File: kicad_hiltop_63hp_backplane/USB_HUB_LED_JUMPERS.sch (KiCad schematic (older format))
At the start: 81 parts, among them J12 4POS_JUMPER, J13 4POS_JUMPER, J14 4POS_JUMPER, J15 4POS_JUMPER, J16 4POS_JUMPER, U5 USB2517, Y2 24Mhz Xtal

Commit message: Rev A
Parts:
- C38, C39, C40, C41, C42, C43, C44, C45, C46, C47, C48, C50, C51, C52, C53: symbol device:C -> hiltop_backplane_brd-rescue:C-device; Devtank (none) -> 105-002
- C49, C54: symbol device:C -> hiltop_backplane_brd-rescue:C-device; Devtank (none) -> 105-014
- D10, D11, D12, D13, D6, D7, D8, D9: value LED -> LED RED; symbol device:LED -> hiltop_backplane_brd-rescue:LED-device; Devtank (none) -> 110-004
- D14, D16, D18, D20, D22, D24, D26: value GRN -> LED GRN; symbol device:LED -> hiltop_backplane_brd-rescue:LED-device; Devtank (none) -> 110-005
- D15, D17, D19, D21, D23, D25, D27: value YEL -> LED YEL; symbol device:LED -> hiltop_backplane_brd-rescue:LED-device; Devtank (none) -> 110-007
- D5: symbol ESD_Protection:NUP2105L -> hiltop_backplane_brd-rescue:NUP2105L-ESD_Protection; Devtank (none) -> 136-002
- J12, J13, J14, J15, J16: symbol gti_Lattice:4POS_JUMPER -> hiltop_backplane_brd-rescue:4POS_JUMPER-gti_Lattice; Devtank (none) -> 711-003
- R48, R49: symbol device:R -> hiltop_backplane_brd-rescue:R-device; Devtank (none) -> 101-015
- R50, R51, R53, R54, R57, R58: symbol device:R -> hiltop_backplane_brd-rescue:R-device; Devtank (none) -> 101-010
- R52: symbol device:R -> hiltop_backplane_brd-rescue:R-device; Devtank (none) -> 101-050
- R55, R56, R59: symbol device:R -> hiltop_backplane_brd-rescue:R-device
- R60, R61, R62, R63, R64, R65, R66, R67, R68, R69, R70, R71, R72, R73, R74, R75, R76, R77, R78, R79, R80, R81: symbol device:R -> hiltop_backplane_brd-rescue:R-device; Devtank (none) -> 101-509
- U5: symbol Devtank:USB2517 -> hiltop_backplane_brd-rescue:USB2517-Devtank; Devtank (none) -> 118-004
- Y2: symbol device:Crystal -> hiltop_backplane_brd-rescue:Crystal-device; Devtank (none) -> 181-003

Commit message: add latest changes
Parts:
- removed D5: NUP2105L, Package_TO_SOT_SMD:SOT-23, symbol hiltop_backplane_brd-rescue:NUP2105L-ESD_Protection
- C38, C43, C44, C45, C46, C47, C48, C49, C50, C51, C52, C53, C54: symbol hiltop_backplane_brd-rescue:C-device -> hiltop_backplane_brd-rescue:C-device-hiltop_backplane_brd-rescue
- C39: value 100nF -> 18pF; symbol hiltop_backplane_brd-rescue:C-device -> hiltop_backplane_brd-rescue:C-device-hiltop_backplane_brd-rescue; Devtank 105-002 -> (none)
- C40, C41: value 100nF -> 1uF; symbol hiltop_backplane_brd-rescue:C-device -> hiltop_backplane_brd-rescue:C-device-hiltop_backplane_brd-rescue; Devtank 105-002 -> (none)
- C42: value 100nF -> 18pF; symbol hiltop_backplane_brd-rescue:C-device -> hiltop_backplane_brd-rescue:C-device-hiltop_backplane_brd-rescue
- D10, D11, D12, D13, D14, D15, D16, D17, D18, D19, D20, D21, D22, D23, D24, D25, D26, D27, D6, D7, D8, D9: symbol hiltop_backplane_brd-rescue:LED-device -> hiltop_backplane_brd-rescue:LED-device-hiltop_backplane_brd-rescue
- J12, J13, J14, J15, J16: symbol hiltop_backplane_brd-rescue:4POS_JUMPER-gti_Lattice -> hiltop_backplane_brd-rescue:4POS_JUMPER-gti_Lattice-hiltop_backplane_brd-rescue
- R48: value 100K -> 0R; symbol hiltop_backplane_brd-rescue:R-device -> hiltop_backplane_brd-rescue:R-device-hiltop_backplane_brd-rescue
- R49, R50, R52, R53, R54, R55, R56, R57, R58, R59, R60, R61, R62, R63, R64, R65, R66, R67, R68, R69, R70, R71, R72, R73, R74, R75, R76, R77, R78, R79, R80, R81: symbol hiltop_backplane_brd-rescue:R-device -> hiltop_backplane_brd-rescue:R-device-hiltop_backplane_brd-rescue
- R51: value 10K -> 1M; symbol hiltop_backplane_brd-rescue:R-device -> hiltop_backplane_brd-rescue:R-device-hiltop_backplane_brd-rescue; Devtank 101-010 -> (none)
- U5: symbol hiltop_backplane_brd-rescue:USB2517-Devtank -> hiltop_backplane_brd-rescue:USB2517-Devtank-hiltop_backplane_brd-rescue
- Y2: symbol hiltop_backplane_brd-rescue:Crystal-device -> hiltop_backplane_brd-rescue:Crystal-device-hiltop_backplane_brd-rescue
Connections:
- wire segments 290 -> 285

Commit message: started simplifications to design
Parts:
- removed J12, J13, J14, J15, J16: 4POS_JUMPER, Connector_PinHeader_2.00mm:PinHeader_2x02_P2.00mm_Vertical, symbol hiltop_backplane_brd-rescue:4POS_JUMPER-gti_Lattice-hiltop_backplane_brd-rescue
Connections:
- net labels removed: EXT_SPI_MISO, EXT_SPI_MOSI, EXT_SPI_SCK, EXT_SPI_SS, FPGA_SPI_DATA1, FPGA_SPI_DATA2, FPGA_SPI_SCK, FPGA_SPI_SDI, FPGA_SPI_SDO, FPGA_SPI_SS, FTDI_AD0_SCK, FTDI_AD1_MOSI, FTDI_AD2_MISO, FTDI_AD3_SS, s_FLASH_MISO, s_FLASH_MOSI, s_FLASH_SCK, s_FLASH_SS
- wire segments 285 -> 265
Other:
- note removed: "Config 1 "="\nFTDI SPI --->FLASH SPI\nEXT SPI ---> FPGA SPI\n\nConfig 2 "||"\nFTDI SPI ---> EXT SPI\nFLASH SPI ---> FPGA SPI"
- note removed: "Switch (FPGA) Master to Slave (M/M)\n"
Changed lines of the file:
@@
 EESchema Schematic File Version 4
-LIBS:hiltop_backplane_brd-cache
-EELAYER 29 0
+EELAYER 30 0
 EELAYER END
 $Descr A4 11693 8268
@@
 Wire Wire Line
 	5625 7250 5425 7250
-$Comp
-L hiltop_backplane_brd-rescue:4POS_JUMPER-gti_Lattice-hiltop_backplane_brd-rescue J12
-U 1 1 5A304A10
-P 3100 5800
-F 0 "J12" H 3100 5800 39  0000 C CNN
-F 1 "4POS_JUMPER" H 3100 5750 39  0000 C CNN
-F 2 "Connector_PinHeader_2.00mm:PinHeader_2x02_P2.00mm_Vertical" H 3100 5800 39  0001 C CNN
-F 3 "" H 3100 5800 39  0001 C CNN
-F 4 "711-003" H 0   0   50  0001 C CNN "Devtank"
-	1    3100 5800
-	1    0    0    -1
-$EndComp
-$Comp
-L hiltop_backplane_brd-rescue:4POS_JUMPER-gti_Lattice-hiltop_backplane_brd-rescue J13
-U 1 1 5A304A17
-P 3100 6150
-F 0 "J13" H 3100 6150 39  0000 C CNN
-F 1 "4POS_JUMPER" H 3100 6100 39  0000 C CNN
-F 2 "Connector_PinHeader_2.00mm:PinHeader_2x02_P2.00mm_Vertical" H 3100 6150 39  0001 C CNN
-F 3 "" H 3100 6150 39  0001 C CNN
-F 4 "711-003" H 0   0   50  0001 C CNN "Devtank"
-	1    3100 6150
-	1    0    0    -1
-$EndComp
-$Comp
-L hiltop_backplane_brd-rescue:4POS_JUMPER-gti_Lattice-hiltop_backplane_brd-rescue J14
-U 1 1 5A304A1E
-P 3100 6550
-F 0 "J14" H 3100 6550 39  0000 C CNN
-F 1 "4POS_JUMPER" H 3100 6500 39  0000 C CNN
-F 2 "Connector_PinHeader_2.00mm:PinHeader_2x02_P2.00mm_Vertical" H 3100 6550 39  0001 C CNN
-F 3 "" H 3100 6550 39  0001 C CNN
-F 4 "711-003" H 0   0   50  0001 C CNN "Devtank"
-	1    3100 6550
-	1    0    0    -1
-$EndComp
-$Comp
-L hiltop_backplane_brd-rescue:4POS_JUMPER-gti_Lattice-hiltop_backplane_brd-rescue J15
-U 1 1 5A304A25
-P 3100 6950
-F 0 "J15" H 3100 6950 39  0000 C CNN
-F 1 "4POS_JUMPER" H 3100 6900 39  0000 C CNN
-F 2 "Connector_PinHeader_2.00mm:PinHeader_2x02_P2.00mm_Vertical" H 3100 6950 39  0001 C CNN
-F 3 "" H 3100 6950 39  0001 C CNN
-F 4 "711-003" H 0   0   50  0001 C CNN "Devtank"
-	1    3100 6950
-	1    0    0    -1
-$EndComp
-Wire Wire Line
-	2700 7100 2850 7100
-Wire Wire Line
-	2700 6700 2850 6700
-Wire Wire Line
-	2700 5950 2850 5950
-Wire Wire Line
-	2700 6300 2850 6300
-Wire Wire Line
-	3350 5950 3500 5950
-Wire Wire Line
-	3350 6300 3500 6300
-Wire Wire Line
-	3350 6700 3500 6700
-Wire Wire Line
-	3350 7100 3500 7100
-Wire Wire Line
-	2700 6050 2850 6050
-Wire Wire Line
-	3350 6050 3950 6050
-Wire Wire Line
-	2700 6400 2850 6400
-Wire Wire Line
-	3350 6400 3950 6400
-Wire Wire Line
-	2700 6800 2850 6800
-Wire Wire Line
-	3350 6800 3500 6800
-Wire Wire Line
-	2700 7200 2850 7200
-Wire Wire Line
-	3350 7200 3500 7200
-$Comp
-L hiltop_backplane_brd-rescue:4POS_JUMPER-gti_Lattice-hiltop_backplane_brd-rescue J16
-U 1 1 5A304A44
-P 3100 7450
-F 0 "J16" H 3100 7450 39  0000 C CNN
-F 1 "4POS_JUMPER" H 3100 7400 39  0000 C CNN
-F 2 "Connector_PinHeader_2.00mm:PinHeader_2x02_P2.00mm_Vertical" H 3100 7450 39  0001 C CNN
-F 3 "" H 3100 7450 39  0001 C CNN
-F 4 "711-003" H 0   0   50  0001 C CNN "Devtank"
-	1    3100 7450
-	1    0    0    -1
-$EndComp
-Wire Wire Line
-	2850 7600 2700 7600
-Wire Wire Line
-	3350 7600 3950 7600
-Wire Wire Line
-	3350 7700 3500 7700
-Wire Wire Line
-	2850 7700 2225 7700
-Text Notes 3750 7400 2    39   ~ 0
-Switch (FPGA) Master to Slave (M/M)\n
-Text Notes 875  7000 0    60   ~ 0
-Config 1 "="\nFTDI SPI --->FLASH SPI\nEXT SPI ---> FPGA SPI\n\nConfig 2 "||"\nFTDI SPI ---> EXT SPI\nFLASH SPI ---> FPGA SPI
 Text HLabel 5425 6050 0    39   Input Italic 8
 LED1
@@
 Text HLabel 5425 7250 0    39   Input Italic 8
 LED7
-Text HLabel 2700 5950 0    39   Input ~ 0
-FTDI_AD2_MISO
-Text HLabel 2700 6050 0    39   Input ~ 0
-EXT_SPI_MISO
-Text HLabel 2700 6300 0    39   Input ~ 0
-FTDI_AD1_MOSI
-Text HLabel 2700 6400 0    39   Input ~ 0
-EXT_SPI_MOSI
-Text HLabel 2700 6700 0    39   Input ~ 0
-FTDI_AD0_SCK
-Text HLabel 2700 6800 0    39   Input ~ 0
-EXT_SPI_SCK
-Text HLabel 2700 7100 0    39   Input ~ 0
-FTDI_AD3_SS
-Text HLabel 2700 7200 0    39   Input ~ 0
-EXT_SPI_SS
-Text HLabel 2700 7600 0    39   Input ~ 0
-FPGA_SPI_SDO
-Text HLabel 3500 5950 2    39   Input ~ 0
-s_FLASH_MOSI
-Text HLabel 3500 6300 2    39   Input ~ 0
-s_FLASH_MISO
-Text HLabel 3500 6700 2    39   Input ~ 0
-s_FLASH_SCK
-Text HLabel 3500 6800 2    39   Input ~ 0
-FPGA_SPI_SCK
-Text HLabel 3500 7200 2    39   Input ~ 0
-FPGA_SPI_SS
-Text HLabel 3500 7700 2    39   Input ~ 0
-FPGA_SPI_SDI
 Text Notes 6225 5750 2    39   Italic 8
 LED 1-7 PULL DOWN
-Text HLabel 3500 7100 2    39   Input ~ 0
-s_FLASH_SS
 $Comp
 L hiltop_backplane_brd-rescue:LED-device-hiltop_backplane_brd-rescue D13
@@
 Text HLabel 1325 1350 0    60   Input ~ 0
 USB_D-
-Text Label 3950 6050 2    28   ~ 0
-FPGA_SPI_DATA1
-Text Label 3950 7600 2    28   ~ 0
-FPGA_SPI_DATA1
-Text Label 2225 7700 0    28   ~ 0
-FPGA_SPI_DATA2
-Text Label 3950 6400 2    28   ~ 0
-FPGA_SPI_DATA2
 Text HLabel 1100 2075 0    60   Input ~ 0
 GND

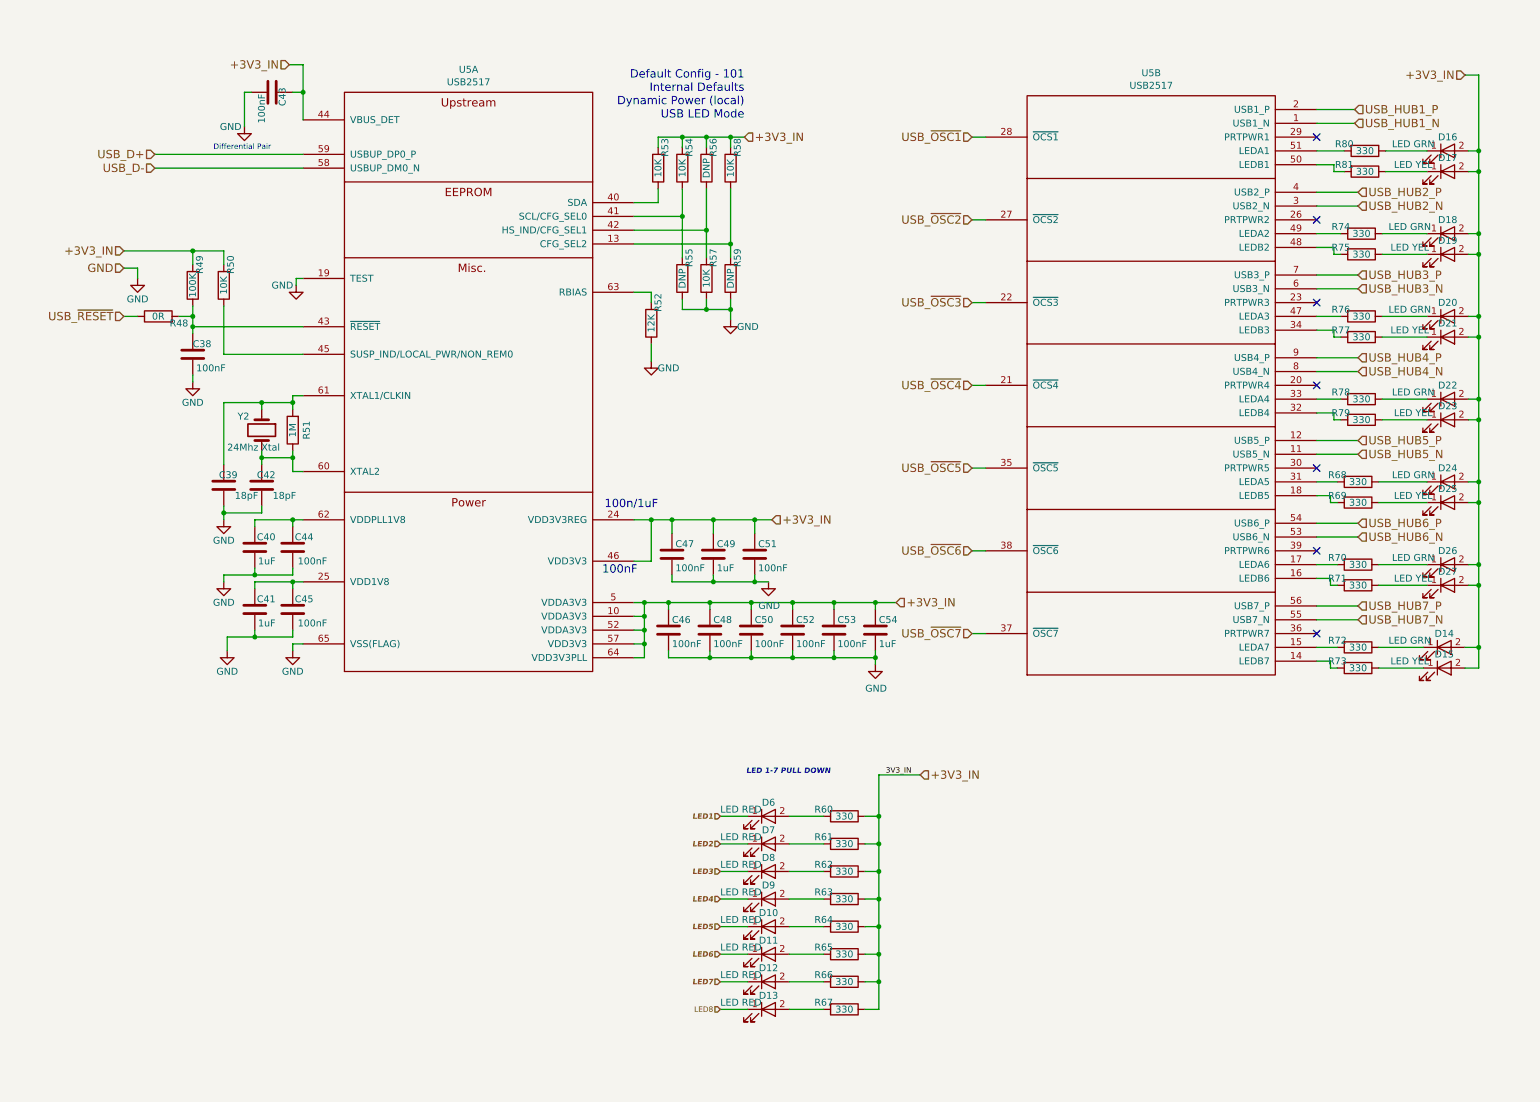
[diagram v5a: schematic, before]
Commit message: updated schematics to RevC including general tidy up
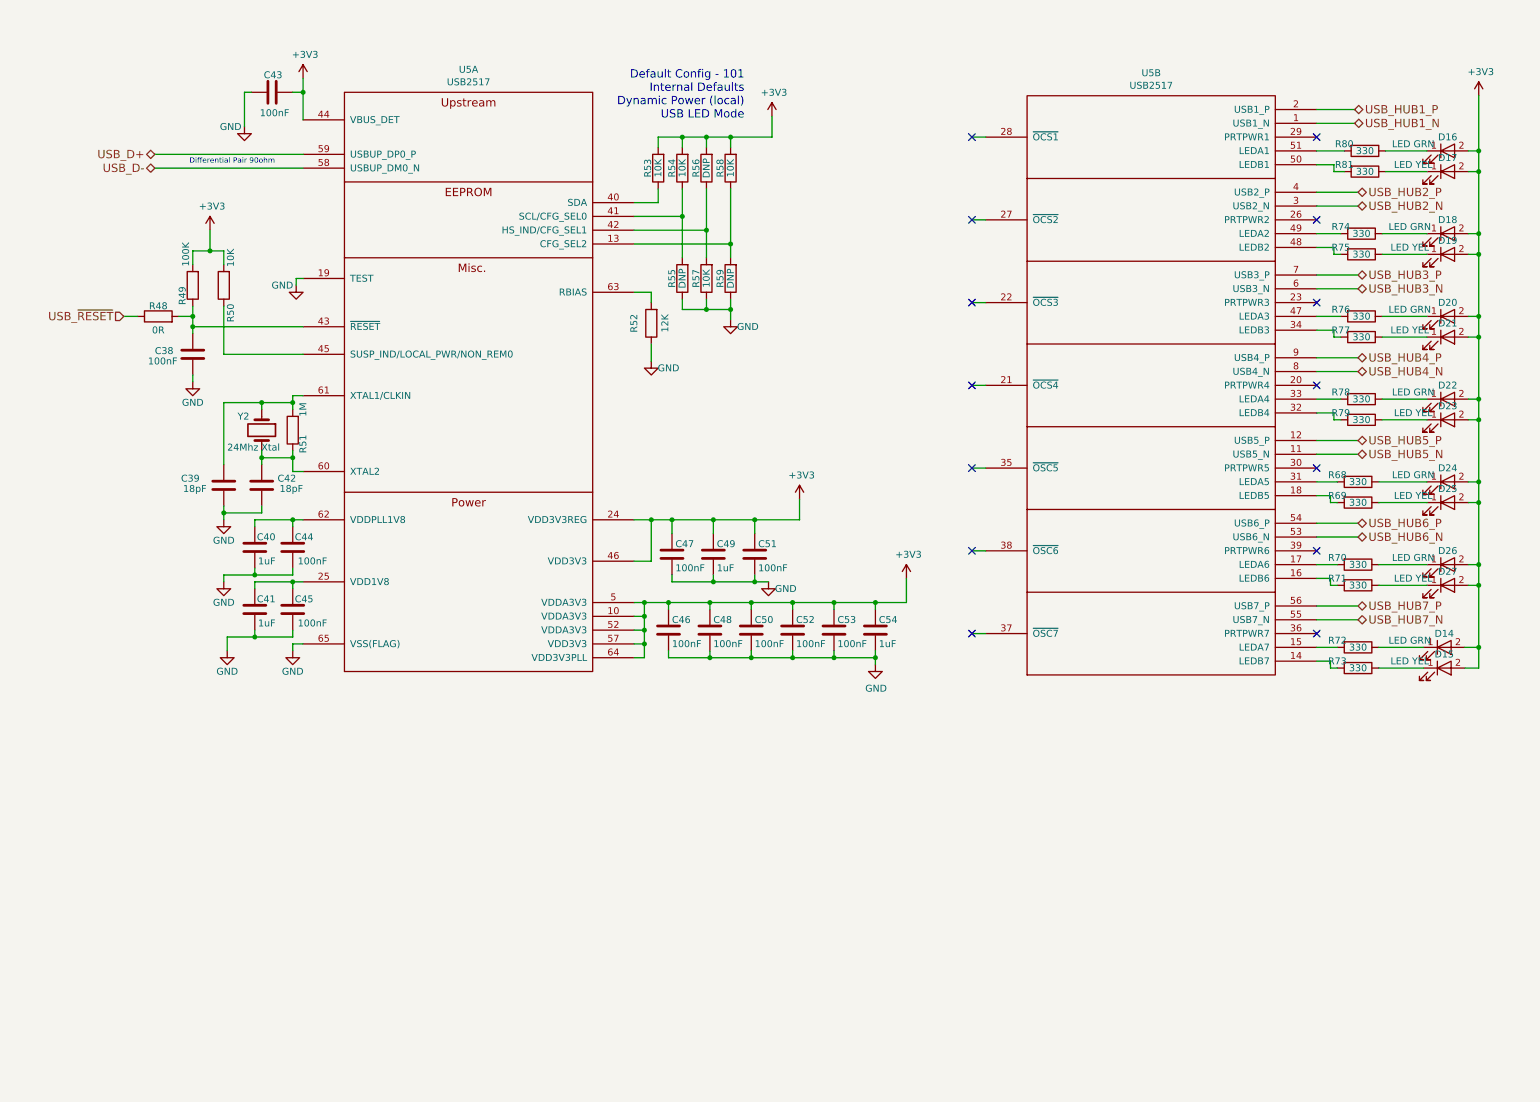
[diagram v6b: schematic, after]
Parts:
- removed D10, D11, D12, D13, D6, D7, D8, D9: LED RED, LED_SMD:LED_0402_1005Metric, symbol hiltop_backplane_brd-rescue:LED-device-hiltop_backplane_brd-rescue
- removed R60, R61, R62, R63, R64, R65, R66, R67: 330, Resistor_SMD:R_0402_1005Metric, symbol hiltop_backplane_brd-rescue:R-device-hiltop_backplane_brd-rescue
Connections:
- net +3V3_IN renamed +3V3
- net USB_~OSC1: no longer names the net of U5.28 (~OCS1)
- net USB_~OSC2: no longer names the net of U5.27 (~OCS2)
- net USB_~OSC3: no longer names the net of U5.22 (~OCS3)
- net USB_~OSC4: no longer names the net of U5.21 (~OCS4)
- net USB_~OSC5: no longer names the net of U5.35 (~OSC5)
- net USB_~OSC6: no longer names the net of U5.38 (~OSC6)
- net USB_~OSC7: no longer names the net of U5.37 (~OSC7)
- no-connect marks 7 -> 14
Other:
- note added: "Differential Pair 90ohm"
- note removed: "100n/1uF"
- note removed: "100nF"
- note removed: "Differential Pair"
- note removed: "LED 1-7 PULL DOWN"
